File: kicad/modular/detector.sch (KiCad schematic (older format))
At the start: 33 parts

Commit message: added more test points to modular, assigned some footprints
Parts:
- removed J?: SIGNAL, symbol Connector_Shield:Shield_2x1x6
- removed J?: POWER, symbol Connector_Shield:Shield_2x1x6
- added J3: HEADER_SIG, symbol Connector_Shield:Shield_2x1x6
- added TP11: I1, TestPoint:TestPoint_THTPad_D1.0mm_Drill0.5mm, symbol Connector:TestPoint
- added TP12: I3, TestPoint:TestPoint_THTPad_D1.0mm_Drill0.5mm, symbol Connector:TestPoint
- added TP13: GND, TestPoint:TestPoint_THTPad_D1.0mm_Drill0.5mm, symbol Connector:TestPoint
- added TP16: I2, TestPoint:TestPoint_THTPad_D1.0mm_Drill0.5mm, symbol Connector:TestPoint
- added TP17: I4, TestPoint:TestPoint_THTPad_D1.0mm_Drill0.5mm, symbol Connector:TestPoint
- added TP7, TP9: +15V, TestPoint:TestPoint_THTPad_D1.0mm_Drill0.5mm, symbol Connector:TestPoint
- added TP8: -15V, TestPoint:TestPoint_THTPad_D1.0mm_Drill0.5mm, symbol Connector:TestPoint
- C10, C11, C12, C13, C14, C15, C16, C7: renamed from C?; footprint (none) -> Capacitor_SMD:C_0603_1608Metric
- C8, C9: renamed from C?; value 5p -> 100n; footprint (none) -> Capacitor_SMD:C_0603_1608Metric
- D5: renamed from D?; footprint (none) -> Sensor_OpticalPosition:S5990
- R5, R6, R7, R8, R9: renamed from R?; footprint (none) -> Resistor_SMD:R_0603_1608Metric
- TP10: renamed from TP?; value TestPoint -> BIAS; footprint (none) -> TestPoint:TestPoint_THTPad_D1.0mm_Drill0.5mm
- TP14: renamed from TP?; value X1 -> U1; footprint (none) -> TestPoint:TestPoint_THTPad_D1.0mm_Drill0.5mm
- TP15: renamed from TP?; value Y1 -> U3; footprint (none) -> TestPoint:TestPoint_THTPad_D1.0mm_Drill0.5mm
- TP18: renamed from TP?; footprint (none) -> TestPoint:TestPoint_THTPad_D1.0mm_Drill0.5mm
- TP19: renamed from TP?; value Y2 -> U4; footprint (none) -> TestPoint:TestPoint_THTPad_D1.0mm_Drill0.5mm
- U3: renamed from U?; footprint (none) -> Package_SO:TSSOP-14_4.4x5mm_P0.65mm
- U4: renamed from U?; footprint Package_SO:MSOP-8_3x3mm_P0.65mm -> Package_SO:SOIC-8_3.9x4.9mm_P1.27mm
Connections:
- wire segments 121 -> 128
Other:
- moved on the sheet: C10, C11, C7, C8, C9, D5E, R5, TP10, U3E

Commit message: completed header footprint, started with pcb design of power board
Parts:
- J3: value HEADER_SIG -> HEADER; footprint (none) -> Connector_Header:PinHeader_2.54mm; symbol Connector_Shield:Shield_2x1x6 -> Connector_Header:Header
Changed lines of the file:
@@
 OPAMP POWER
 $Comp
-L Connector_Shield:Shield_2x1x6 J3
+L Connector_Header:Header J3
 U 1 1 5D7EC537
 P 2200 1300
 F 0 "J3" H 2350 1250 50  0000 C CNN
-F 1 "HEADER_SIG" H 2350 100 50  0000 C CNN
-F 2 "" H 2200 1300 50  0001 C CNN
+F 1 "HEADER" H 2350 100 50  0000 C CNN
+F 2 "Connector_Header:PinHeader_2.54mm" H 2200 1300 50  0001 C CNN
 F 3 "" H 2200 1300 50  0001 C CNN
 	1    2200 1300
@@
 $EndComp
 $Comp
-L Connector_Shield:Shield_2x1x6 J3
+L Connector_Header:Header J3
 U 2 1 5D7EFB55
 P 8900 1050
 F 0 "J3" H 9000 1000 50  0000 L CNN
-F 1 "HEADER_SIG" H 8850 -150 50  0000 L CNN
-F 2 "" H 8900 1050 50  0001 C CNN
+F 1 "HEADER" H 8950 -150 50  0000 L CNN
+F 2 "Connector_Header:PinHeader_2.54mm" H 8900 1050 50  0001 C CNN
 F 3 "" H 8900 1050 50  0001 C CNN
 	2    8900 1050

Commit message: completed detector board
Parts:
- removed TP11: I1, TestPoint:TestPoint_THTPad_D1.0mm_Drill0.5mm, symbol Connector:TestPoint
- removed TP12: I3, TestPoint:TestPoint_THTPad_D1.0mm_Drill0.5mm, symbol Connector:TestPoint
- removed TP14: U1, TestPoint:TestPoint_THTPad_D1.0mm_Drill0.5mm, symbol Connector:TestPoint
- removed TP15: U3, TestPoint:TestPoint_THTPad_D1.0mm_Drill0.5mm, symbol Connector:TestPoint
- removed TP16: I2, TestPoint:TestPoint_THTPad_D1.0mm_Drill0.5mm, symbol Connector:TestPoint
- removed TP17: I4, TestPoint:TestPoint_THTPad_D1.0mm_Drill0.5mm, symbol Connector:TestPoint
- removed TP18: X2, TestPoint:TestPoint_THTPad_D1.0mm_Drill0.5mm, symbol Connector:TestPoint
- removed TP19: U4, TestPoint:TestPoint_THTPad_D1.0mm_Drill0.5mm, symbol Connector:TestPoint
- TP7: value +15V -> +12V
- TP8: value -15V -> -12V
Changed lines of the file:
@@
 	5650 2450 5400 2450
 Connection ~ 5400 2450
-$Comp
-L Connector:TestPoint TP14
-U 1 1 5D4ED18A
-P 5400 2650
-F 0 "TP14" H 5342 2676 50  0000 R CNN
-F 1 "U1" H 5342 2767 50  0000 R CNN
-F 2 "TestPoint:TestPoint_THTPad_D1.0mm_Drill0.5mm" H 5600 2650 50  0001 C CNN
-F 3 "~" H 5600 2650 50  0001 C CNN
-	1    5400 2650
-	-1   0    0    1
-$EndComp
 Wire Wire Line
 	5400 1350 5400 1850
 Connection ~ 5400 1850
-Wire Wire Line
-	5400 2450 5400 2650
 Wire Wire Line
 	6250 2350 6400 2350
@@
 	7650 2450 7400 2450
 Connection ~ 7400 2450
-$Comp
-L Connector:TestPoint TP18
-U 1 1 5D4FA6CC
-P 7400 2650
-F 0 "TP18" H 7342 2676 50  0000 R CNN
-F 1 "X2" H 7342 2767 50  0000 R CNN
-F 2 "TestPoint:TestPoint_THTPad_D1.0mm_Drill0.5mm" H 7600 2650 50  0001 C CNN
-F 3 "~" H 7600 2650 50  0001 C CNN
-	1    7400 2650
-	-1   0    0    1
-$EndComp
 Wire Wire Line
 	7400 1350 7400 1850
 Connection ~ 7400 1850
-Wire Wire Line
-	7400 2450 7400 2650
 $Comp
 L Sensor_OpticalPosition:S599x D5
@@
 	5650 4400 5400 4400
 Connection ~ 5400 4400
-$Comp
-L Connector:TestPoint TP15
-U 1 1 5D506748
-P 5400 4600
-F 0 "TP15" H 5342 4626 50  0000 R CNN
-F 1 "U3" H 5342 4717 50  0000 R CNN
-F 2 "TestPoint:TestPoint_THTPad_D1.0mm_Drill0.5mm" H 5600 4600 50  0001 C CNN
-F 3 "~" H 5600 4600 50  0001 C CNN
-	1    5400 4600
-	-1   0    0    1
-$EndComp
 Wire Wire Line
 	5400 3300 5400 3800
 Connection ~ 5400 3800
-Wire Wire Line
-	5400 4400 5400 4600
 Wire Wire Line
 	6250 4300 6400 4300
@@
 	7650 4400 7400 4400
 Connection ~ 7400 4400
-$Comp
-L Connector:TestPoint TP19
-U 1 1 5D506774
-P 7400 4600
-F 0 "TP19" H 7342 4626 50  0000 R CNN
-F 1 "U4" H 7342 4717 50  0000 R CNN
-F 2 "TestPoint:TestPoint_THTPad_D1.0mm_Drill0.5mm" H 7600 4600 50  0001 C CNN
-F 3 "~" H 7600 4600 50  0001 C CNN
-	1    7400 4600
-	-1   0    0    1
-$EndComp
 Wire Wire Line
 	7400 3300 7400 3800
 Connection ~ 7400 3800
-Wire Wire Line
-	7400 4400 7400 4600
 $Comp
 L Device:Opamp_Quad_Generic U3
@@
 P 2050 3800
 F 0 "TP7" V 2245 3872 50  0000 C CNN
-F 1 "+15V" V 2154 3872 50  0000 C CNN
+F 1 "+12V" V 2154 3872 50  0000 C CNN
 F 2 "TestPoint:TestPoint_THTPad_D1.0mm_Drill0.5mm" H 2250 3800 50  0001 C CNN
 F 3 "~" H 2250 3800 50  0001 C CNN
@@
 P 2050 4700
 F 0 "TP8" V 2245 4772 50  0000 C CNN
-F 1 "-15V" V 2154 4772 50  0000 C CNN
+F 1 "-12V" V 2154 4772 50  0000 C CNN
 F 2 "TestPoint:TestPoint_THTPad_D1.0mm_Drill0.5mm" H 2250 4700 50  0001 C CNN
 F 3 "~" H 2250 4700 50  0001 C CNN
@@
 Wire Wire Line
 	2050 4700 2300 4700
-$Comp
-L Connector:TestPoint TP11
-U 1 1 5D90397B
-P 4200 1850
-F 0 "TP11" V 4395 1922 50  0000 C CNN
-F 1 "I1" V 4304 1922 50  0000 C CNN
-F 2 "TestPoint:TestPoint_THTPad_D1.0mm_Drill0.5mm" H 4400 1850 50  0001 C CNN
-F 3 "~" H 4400 1850 50  0001 C CNN
-	1    4200 1850
-	0    -1   -1   0
-$EndComp
-Wire Wire Line
-	4200 1850 4400 1850
-$Comp
-L Connector:TestPoint TP16
-U 1 1 5D90A09A
-P 6250 1850
-F 0 "TP16" V 6445 1922 50  0000 C CNN
-F 1 "I2" V 6354 1922 50  0000 C CNN
-F 2 "TestPoint:TestPoint_THTPad_D1.0mm_Drill0.5mm" H 6450 1850 50  0001 C CNN
-F 3 "~" H 6450 1850 50  0001 C CNN
-	1    6250 1850
-	0    -1   -1   0
-$EndComp
-Wire Wire Line
-	6250 1850 6400 1850
-$Comp
-L Connector:TestPoint TP12
-U 1 1 5D90FE8E
-P 4250 3800
-F 0 "TP12" V 4445 3872 50  0000 C CNN
-F 1 "I3" V 4354 3872 50  0000 C CNN
-F 2 "TestPoint:TestPoint_THTPad_D1.0mm_Drill0.5mm" H 4450 3800 50  0001 C CNN
-F 3 "~" H 4450 3800 50  0001 C CNN
-	1    4250 3800
-	0    -1   -1   0
-$EndComp
-Wire Wire Line
-	4250 3800 4400 3800
-$Comp
-L Connector:TestPoint TP17
-U 1 1 5D915B17
-P 6250 3800
-F 0 "TP17" V 6445 3872 50  0000 C CNN
-F 1 "I4" V 6354 3872 50  0000 C CNN
-F 2 "TestPoint:TestPoint_THTPad_D1.0mm_Drill0.5mm" H 6450 3800 50  0001 C CNN
-F 3 "~" H 6450 3800 50  0001 C CNN
-	1    6250 3800
-	0    -1   -1   0
-$EndComp
-Wire Wire Line
-	6250 3800 6400 3800
 $EndSCHEMATC

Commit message: started redesign of pcb
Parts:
- removed TP13: GND, TestPoint:TestPoint_THTPad_D1.0mm_Drill0.5mm, symbol Connector:TestPoint
- removed TP9: +15V, TestPoint:TestPoint_THTPad_D1.0mm_Drill0.5mm, symbol Connector:TestPoint
- renumbered TP7 to TP1, TP8 to TP2, TP10 to TP3
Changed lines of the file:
@@
 	4350 6700 4350 6300
 $Comp
-L Connector:TestPoint TP10
+L Connector:TestPoint TP3
 U 1 1 5D5B0543
 P 4100 6200
-F 0 "TP10" H 4158 6318 50  0000 L CNN
+F 0 "TP3" H 4158 6318 50  0000 L CNN
 F 1 "BIAS" H 4158 6227 50  0000 L CNN
 F 2 "TestPoint:TestPoint_THTPad_D1.0mm_Drill0.5mm" H 4300 6200 50  0001 C CNN
@@
 	2500 2000 2600 2100
 $Comp
-L Connector:TestPoint TP9
-U 1 1 5D8C8343
-P 2350 6200
-F 0 "TP9" H 2408 6318 50  0000 L CNN
-F 1 "+15V" H 2408 6227 50  0000 L CNN
-F 2 "TestPoint:TestPoint_THTPad_D1.0mm_Drill0.5mm" H 2550 6200 50  0001 C CNN
-F 3 "~" H 2550 6200 50  0001 C CNN
-	1    2350 6200
-	1    0    0    -1
-$EndComp
-Wire Wire Line
-	2350 6200 2350 6300
-$Comp
-L Connector:TestPoint TP13
-U 1 1 5D8E6790
-P 4550 7300
-F 0 "TP13" V 4504 7488 50  0000 L CNN
-F 1 "GND" V 4595 7488 50  0000 L CNN
-F 2 "TestPoint:TestPoint_THTPad_D1.0mm_Drill0.5mm" H 4750 7300 50  0001 C CNN
-F 3 "~" H 4750 7300 50  0001 C CNN
-	1    4550 7300
-	0    1    1    0
-$EndComp
-Wire Wire Line
-	4550 7300 4350 7300
-Connection ~ 4350 7300
-$Comp
-L Connector:TestPoint TP7
+L Connector:TestPoint TP1
 U 1 1 5D8EC494
 P 2050 3800
-F 0 "TP7" V 2245 3872 50  0000 C CNN
+F 0 "TP1" V 2245 3872 50  0000 C CNN
 F 1 "+12V" V 2154 3872 50  0000 C CNN
 F 2 "TestPoint:TestPoint_THTPad_D1.0mm_Drill0.5mm" H 2250 3800 50  0001 C CNN
@@
 	2050 3800 2300 3800
 $Comp
-L Connector:TestPoint TP8
+L Connector:TestPoint TP2
 U 1 1 5D8F1FF0
 P 2050 4700
-F 0 "TP8" V 2245 4772 50  0000 C CNN
+F 0 "TP2" V 2245 4772 50  0000 C CNN
 F 1 "-12V" V 2154 4772 50  0000 C CNN
 F 2 "TestPoint:TestPoint_THTPad_D1.0mm_Drill0.5mm" H 2250 4700 50  0001 C CNN

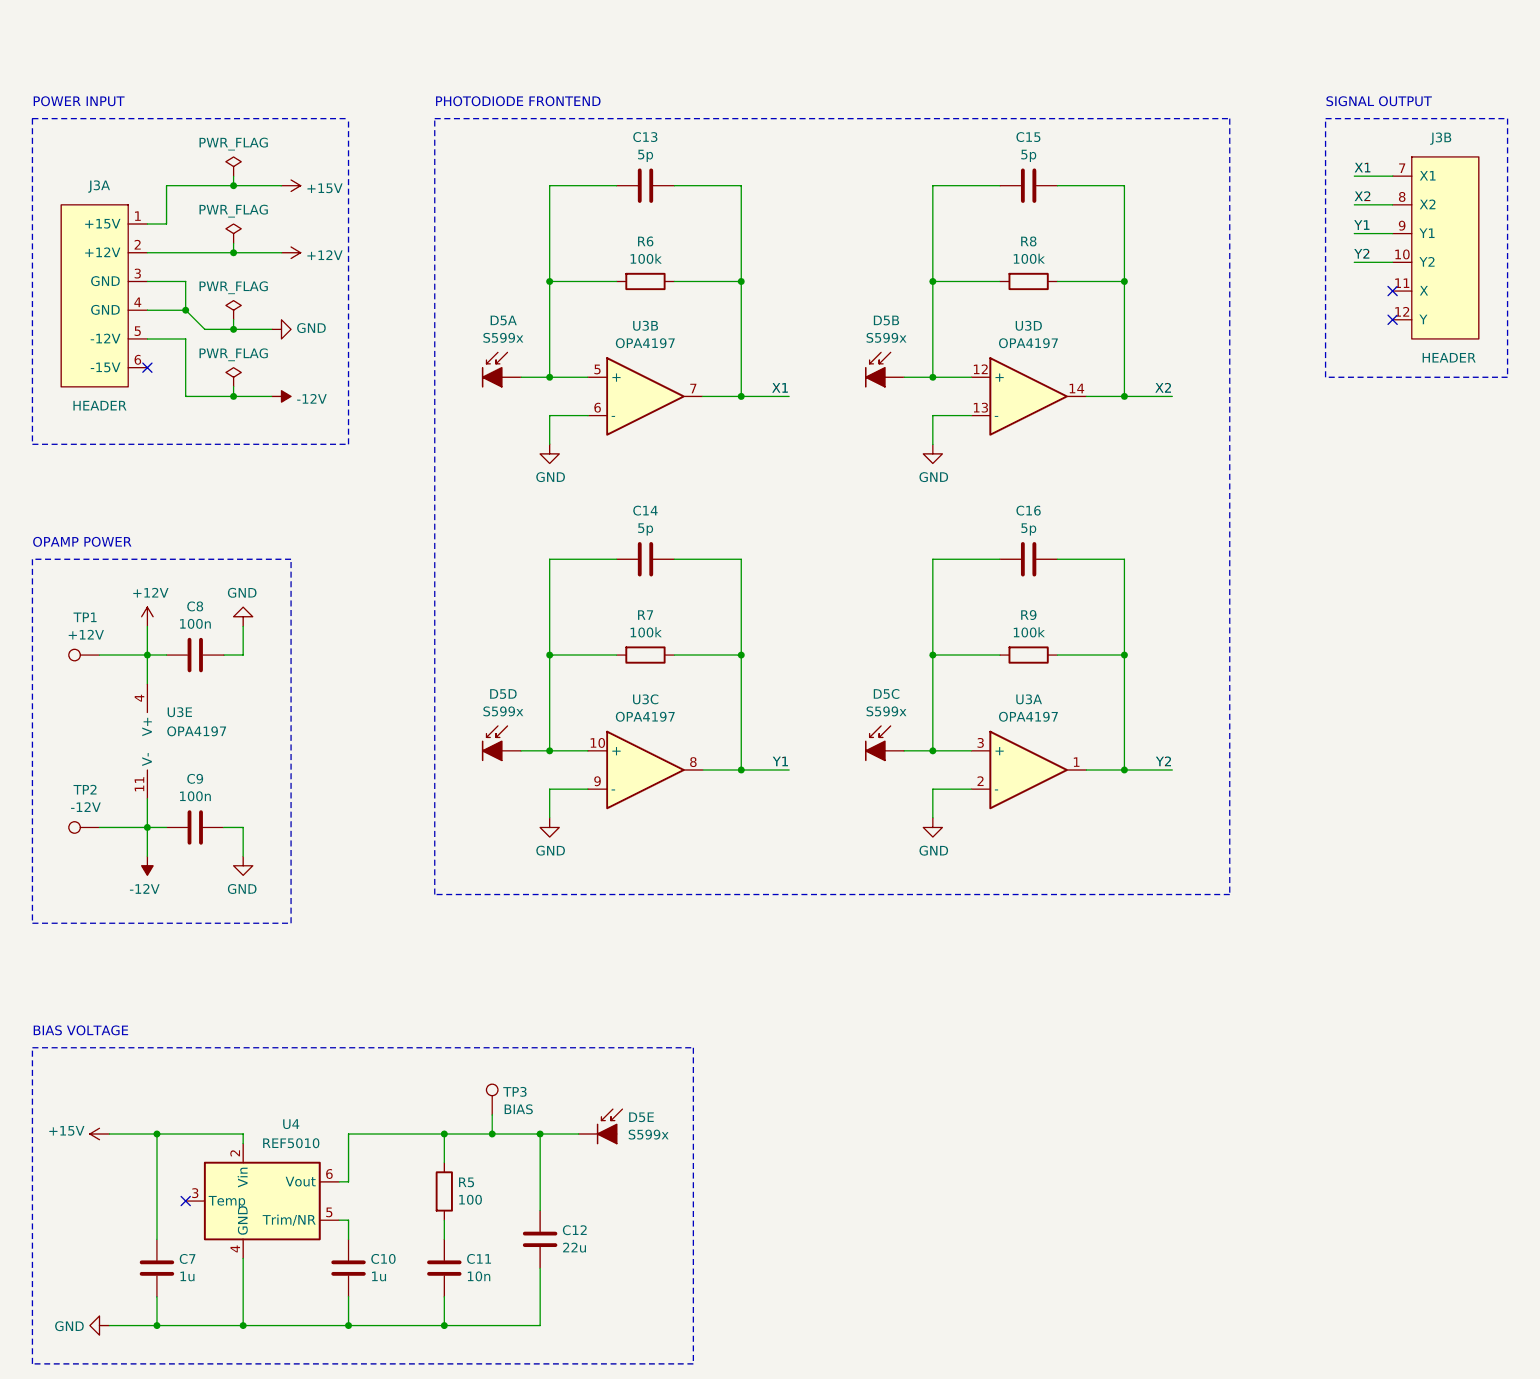
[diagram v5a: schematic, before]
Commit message: redesigned pcb with more symmetry
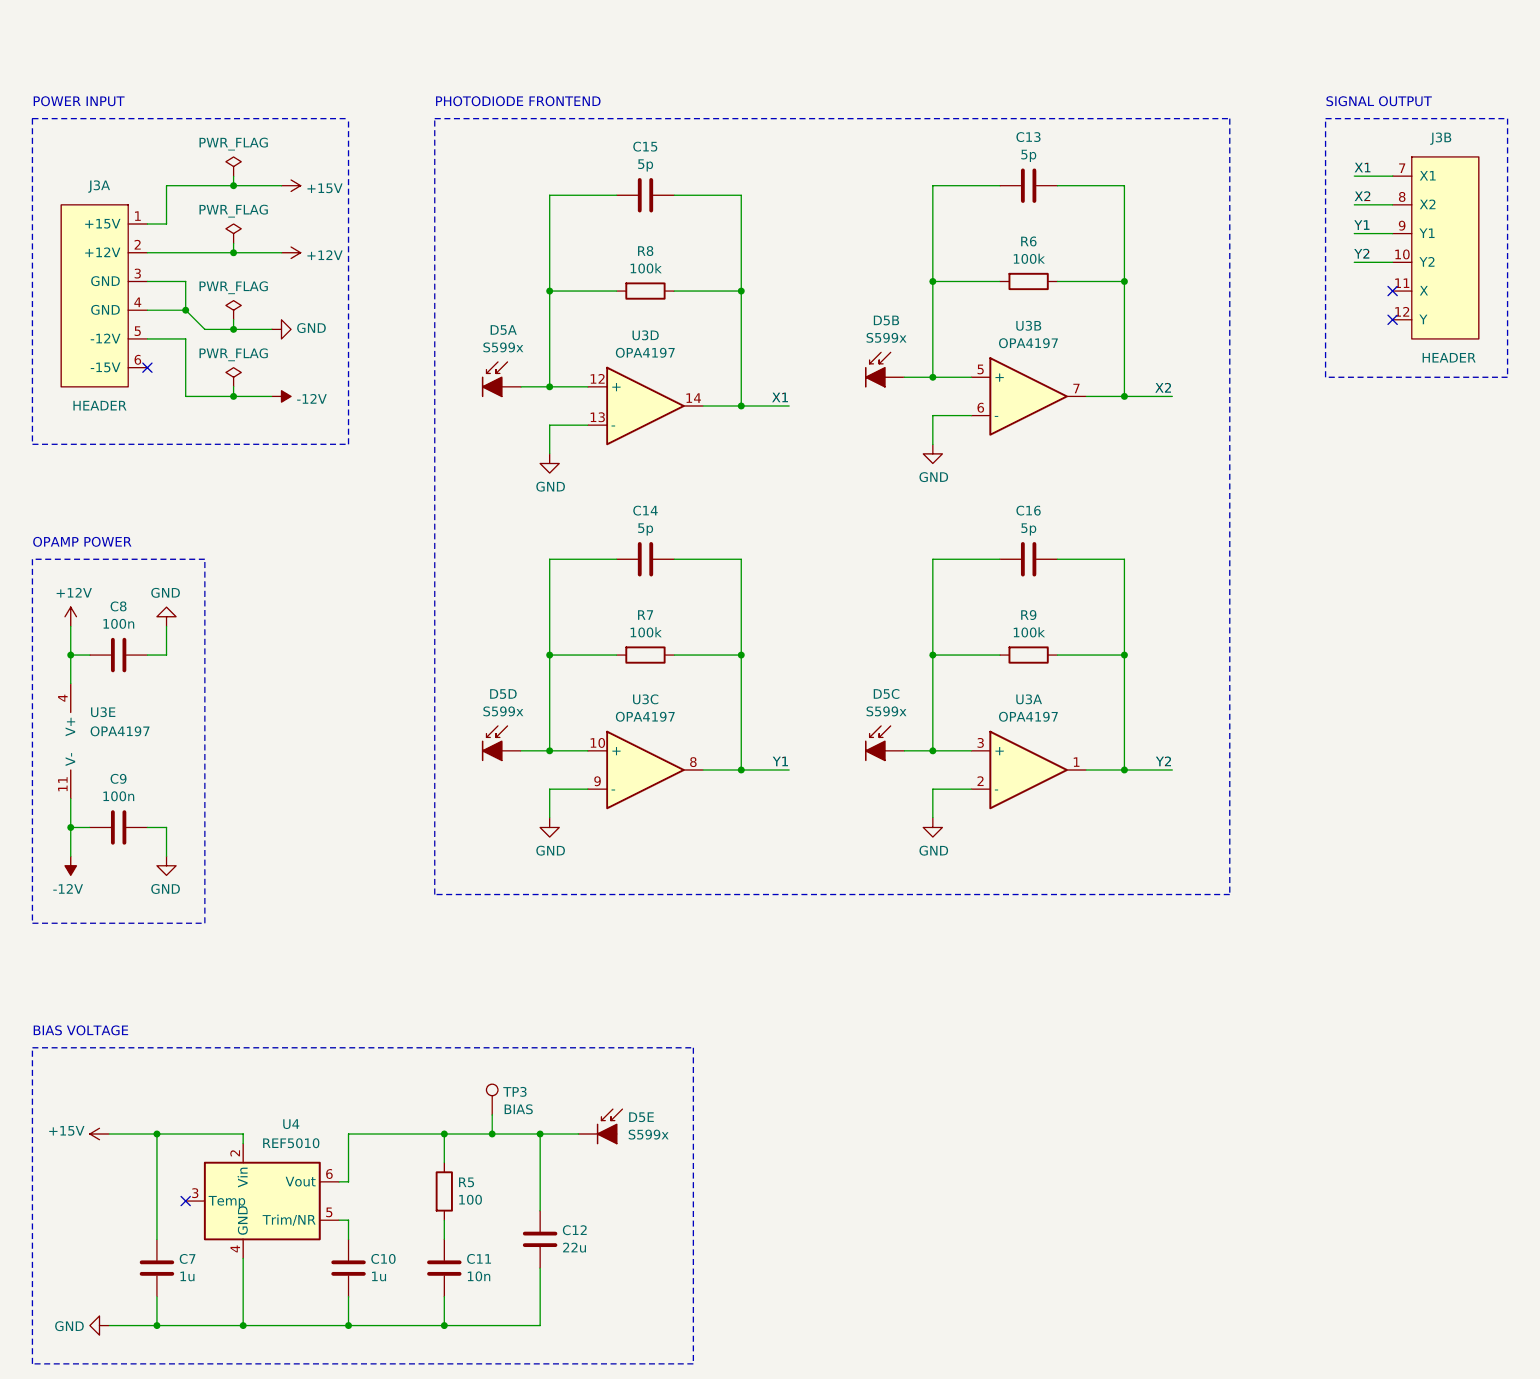
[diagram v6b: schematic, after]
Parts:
- removed TP1: +12V, TestPoint:TestPoint_THTPad_D1.0mm_Drill0.5mm, symbol Connector:TestPoint
- removed TP2: -12V, TestPoint:TestPoint_THTPad_D1.0mm_Drill0.5mm, symbol Connector:TestPoint
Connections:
- net X1: now also C15.1, R8.1, U3.14; no longer C13.1, R6.1, U3.7
- net X2: now also C13.1, R6.1, U3.7; no longer C15.1, R8.1, U3.14
- net at C13.2, R6.2, U3.5 (+): now also D5.6 (I2); no longer D5.1 (I1)
- net at C15.2, R8.2, U3.12 (+): now also D5.1 (I1); no longer D5.6 (I2)
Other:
- moved on the sheet: C13, C15, C8, C9, D5A, R6, R8, U3B, U3D, U3E
